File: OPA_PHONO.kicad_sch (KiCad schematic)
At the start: 3 parts, among them J1 Barrel_Jack, J2 Conn_Coaxial_x2, J3 Conn_Coaxial_x2

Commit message: CHANGE POWER SUPPLY
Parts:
- removed J1: Barrel_Jack, Connector_BarrelJack:BarrelJack_CUI_PJ-063AH_Horizontal, symbol Connector:Barrel_Jack
- added J4: USB_C_Receptacle_USB2.0, Connector_USB:USB_C_Receptacle_JAE_DX07S016JA1R1500, symbol Connector:USB_C_Receptacle_USB2.0
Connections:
- net GND: now also J4.A1 (GND), J4.A12 (GND), J4.B1 (GND), J4.B12 (GND), J4.S1 (SHIELD)
- new net POWER/VIN: J4.A4 (VBUS), J4.A9 (VBUS), J4.B4 (VBUS), J4.B9 (VBUS)
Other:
- sheet POWER ports: added VIN; removed AC_A, AC_B

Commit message: update layout
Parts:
- removed J2, J3: Conn_Coaxial_x2, OPA_PHONO:PJRAS2X1S01X, symbol Connector:Conn_Coaxial_x2
- added J1, J2: PJRAS2X1S01X, OPA_PHONO:PJRAS2X1S01X, symbol OPA_PHONO:PJRAS2X1S01X
- J4: value USB_C_Receptacle_USB2.0 -> UJC-HP-3-SMT-TR; footprint Connector_USB:USB_C_Receptacle_JAE_DX07S016JA1R1500 -> Connector_USB:USB_C_Receptacle_Palconn_UTC16-G
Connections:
- net GND: now also J1.S1, J1.S2, J2.S1, J2.S2
- net IN_L: now also J2.T1
- net IN_R: now also J2.T2
- net OUT_L: now also J1.T1
- net OUT_R: now also J1.T2

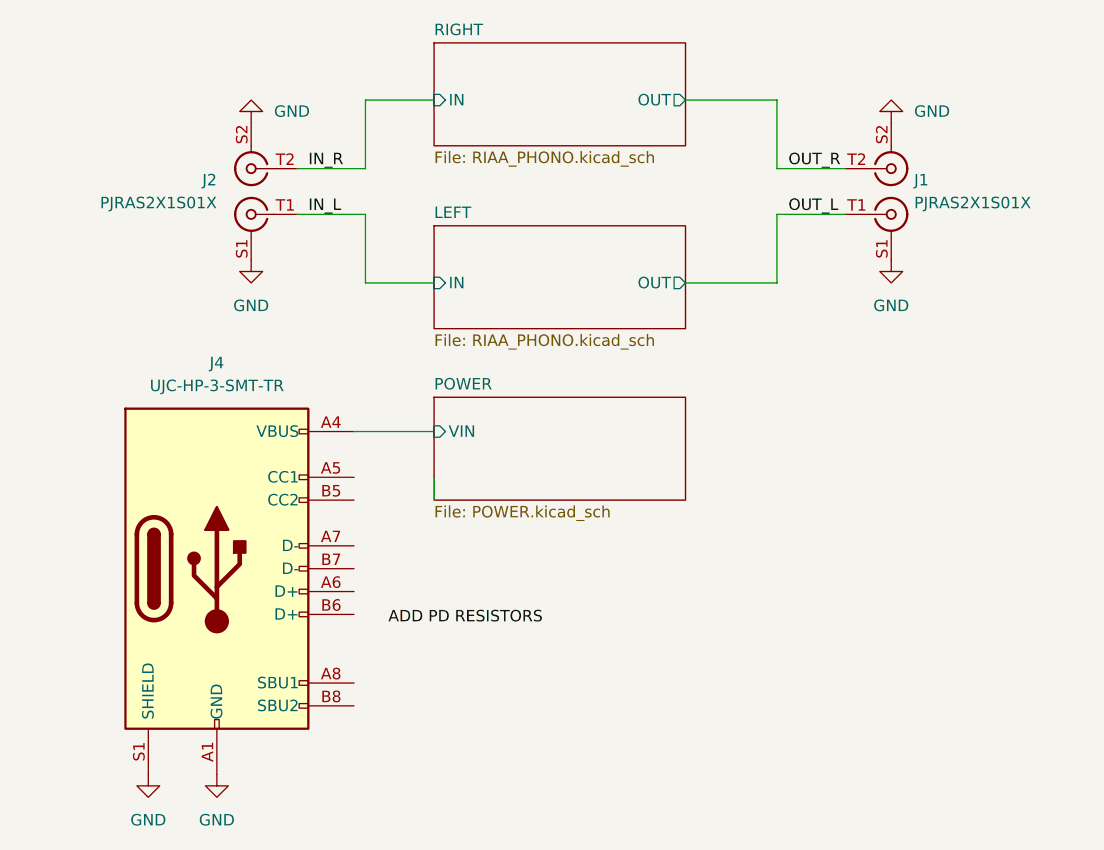
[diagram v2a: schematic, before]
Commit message: add usb c connector
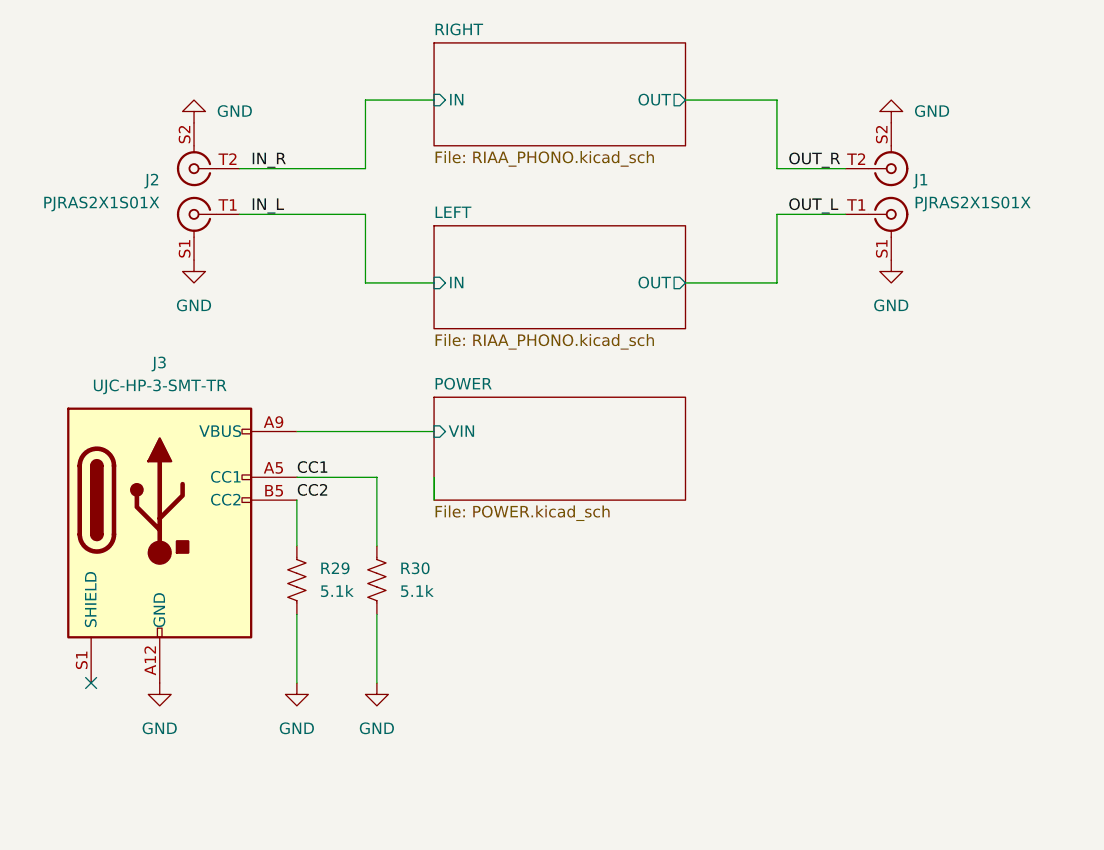
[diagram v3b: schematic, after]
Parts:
- removed J4: UJC-HP-3-SMT-TR, Connector_USB:USB_C_Receptacle_Palconn_UTC16-G, symbol Connector:USB_C_Receptacle_USB2.0
- added J3: UJC-HP-3-SMT-TR, OPA_PHONO:CUI_UJC-HP-3-SMT-TR, symbol OPA_PHONO:UJC-HP-3-SMT-TR
- added R29, R30: 5.1k, Resistor_SMD:R_0402_1005Metric, symbol Device:R_US
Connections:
- net GND: now also J3.A12 (GND), J3.B12 (GND), R29.2, R30.2
- net POWER/VIN: now also J3.A9 (VBUS), J3.B9 (VBUS)
- new net: J3.24 (SHIELD), J3.S1 (SHIELD), J3.S2 (SHIELD), J3.S3 (SHIELD)
- new net CC1: J3.A5 (CC1), R30.1
- new net CC2: J3.B5 (CC2), R29.1
- no-connect marks 0 -> 1
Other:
- moved on the sheet: J2

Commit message: Update component fields
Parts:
- J1, J2: MPN (none) -> PJRAS2X1S01X; Manufacturer (none) -> Switchcraft Inc.
- J3: MPN (none) -> UJC-HP-3-SMT-TR; Manufacturer (none) -> CUI Devices
- R29, R30: MPN (none) -> RC0402FR-075K1L; Manufacturer (none) -> YAGEO
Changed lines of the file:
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@@
+      (effects (font (size 1.27 1.27)) hide)
+    )
+    (property "Description" "CONN DUAL RCA JACK MONO 3.2MM R/A" (id 4) (at 209.55 72.39 0)
+      (effects (font (size 1.27 1.27)) hide)
+    )
+    (property "MPN" "PJRAS2X1S01X" (id 5) (at 209.55 72.39 0)
+      (effects (font (size 1.27 1.27)) hide)
+    )
+    (property "Manufacturer" "Switchcraft Inc." (id 6) (at 209.55 72.39 0)
       (effects (font (size 1.27 1.27)) hide)
     )
@@
       (effects (font (size 1.27 1.27)) hide)
     )
+    (property "Description" "RES SMD 5.1K OHM 1% 1/16W 0402" (id 4) (at 152.4 115.57 0)
+      (effects (font (size 1.27 1.27)) hide)
+    )
+    (property "MPN" "RC0402FR-075K1L" (id 5) (at 152.4 115.57 0)
+      (effects (font (size 1.27 1.27)) hide)
+    )
+    (property "Manufacturer" "YAGEO" (id 6) (at 152.4 115.57 0)
+      (effects (font (size 1.27 1.27)) hide)
+    )
     (pin "1")
     (pin "2")
@@
     )
     (property "Datasheet" "~" (id 3) (at 143.51 115.57 0)
+      (effects (font (size 1.27 1.27)) hide)
+    )
+    (property "Description" "RES SMD 5.1K OHM 1% 1/16W 0402" (id 4) (at 143.51 115.57 0)
+      (effects (font (size 1.27 1.27)) hide)
+    )
+    (property "MPN" "RC0402FR-075K1L" (id 5) (at 143.51 115.57 0)
+      (effects (font (size 1.27 1.27)) hide)
+    )
+    (property "Manufacturer" "YAGEO" (id 6) (at 143.51 115.57 0)
       (effects (font (size 1.27 1.27)) hide)
     )
@@
     )
     (property "Datasheet" "https://www.usb.org/sites/default/files/documents/usb_type-c.zip" (id 3) (at 130.81 104.14 0)
+      (effects (font (size 1.27 1.27)) hide)
+    )
+    (property "Description" "CONN RCPT TYPE C 24POS SMD RA" (id 4) (at 128.27 114.3 0)
+      (effects (font (size 1.27 1.27)) hide)
+    )
+    (property "MPN" "UJC-HP-3-SMT-TR" (id 5) (at 128.27 114.3 0)
+      (effects (font (size 1.27 1.27)) hide)
+    )
+    (property "Manufacturer" "CUI Devices" (id 6) (at 128.27 114.3 0)
       (effects (font (size 1.27 1.27)) hide)
     )
@@
       (effects (font (size 1.27 1.27)) hide)
     )
+    (property "Description" "CONN DUAL RCA JACK MONO 3.2MM R/A" (id 4) (at 132.08 72.39 0)
+      (effects (font (size 1.27 1.27)) hide)
+    )
+    (property "MPN" "PJRAS2X1S01X" (id 5) (at 132.08 72.39 0)
+      (effects (font (size 1.27 1.27)) hide)
+    )
+    (property "Manufacturer" "Switchcraft Inc." (id 6) (at 132.08 72.39 0)
+      (effects (font (size 1.27 1.27)) hide)
+    )
     (pin "S2")
     (pin "T1")
@@
     )
     (path "/b71452ae-e2ec-4238-9d16-71d9677f964c/3401a4bc-8750-45f7-8ad3-ee304a81e512"
-      (reference "C2") (unit 1) (value "68n") (footprint "Capacitor_SMD:C_1206_3216Metric")
+      (reference "C2") (unit 1) (value "68n") (footprint "Capacitor_SMD:C_1210_3225Metric")
     )
     (path "/b71452ae-e2ec-4238-9d16-71d9677f964c/e7e337ea-d0d4-4479-a2c0-823fa5bff63a"
-      (reference "C3") (unit 1) (value "68n") (footprint "Capacitor_SMD:C_1206_3216Metric")
+      (reference "C3") (unit 1) (value "68n") (footprint "Capacitor_SMD:C_1210_3225Metric")
     )
     (path "/b71452ae-e2ec-4238-9d16-71d9677f964c/47e616e0-9f9d-4905-87b6-b1f7ea1d9240"
@@
     )
     (path "/c67bced7-2ecb-4fda-afd4-a12d6372c9ce/3401a4bc-8750-45f7-8ad3-ee304a81e512"
-      (reference "C8") (unit 1) (value "68n") (footprint "Capacitor_SMD:C_1206_3216Metric")
+      (reference "C8") (unit 1) (value "68n") (footprint "Capacitor_SMD:C_1210_3225Metric")
     )
     (path "/c67bced7-2ecb-4fda-afd4-a12d6372c9ce/e7e337ea-d0d4-4479-a2c0-823fa5bff63a"
-      (reference "C9") (unit 1) (value "68n") (footprint "Capacitor_SMD:C_1206_3216Metric")
+      (reference "C9") (unit 1) (value "68n") (footprint "Capacitor_SMD:C_1210_3225Metric")
     )
     (path "/c67bced7-2ecb-4fda-afd4-a12d6372c9ce/47e616e0-9f9d-4905-87b6-b1f7ea1d9240"
@@
     )
     (path "/54617677-cfc6-4c88-8682-59d8a487d34d/012ce2e0-2b16-46fe-aa72-a30f8cf3f1ba"
-      (reference "C19") (unit 1) (value "1u") (footprint "Capacitor_SMD:C_0402_1005Metric")
+      (reference "C19") (unit 1) (value "4.7u") (footprint "Capacitor_SMD:C_0402_1005Metric")
     )
     (path "/54617677-cfc6-4c88-8682-59d8a487d34d/8b3b6e42-30ae-4787-975f-1307bbc78122"
-      (reference "C20") (unit 1) (value "1u") (footprint "Capacitor_SMD:C_0402_1005Metric")
+      (reference "C20") (unit 1) (value "4.7u") (footprint "Capacitor_SMD:C_0402_1005Metric")
     )
     (path "/54617677-cfc6-4c88-8682-59d8a487d34d/b865ef55-d049-44bf-9f62-477ce371aff2"
-      (reference "C21") (unit 1) (value "1u") (footprint "Capacitor_SMD:C_0402_1005Metric")
+      (reference "C21") (unit 1) (value "4.7u") (footprint "Capacitor_SMD:C_0402_1005Metric")
     )
     (path "/54617677-cfc6-4c88-8682-59d8a487d34d/7481d368-de94-4cfa-8658-752acc214285"
-      (reference "C22") (unit 1) (value "1u") (footprint "Capacitor_SMD:C_0402_1005Metric")
+      (reference "C22") (unit 1) (value "4.7u") (footprint "Capacitor_SMD:C_0402_1005Metric")
     )
     (path "/54617677-cfc6-4c88-8682-59d8a487d34d/d015ac9c-8503-428f-b611-918e99cff21b"
@@
     )
     (path "/b71452ae-e2ec-4238-9d16-71d9677f964c/2a4ad1e3-8d24-4e7f-868b-1019aa3d2553"
-      (reference "R1") (unit 1) (value "R_US") (footprint "Resistor_SMD:R_0402_1005Metric")
+      (reference "R1") (unit 1) (value "47k") (footprint "Resistor_SMD:R_0402_1005Metric")
     )
     (path "/b71452ae-e2ec-4238-9d16-71d9677f964c/b777cf12-c2ab-48a2-93f0-242f456945c9"
@@
     )
     (path "/c67bced7-2ecb-4fda-afd4-a12d6372c9ce/2a4ad1e3-8d24-4e7f-868b-1019aa3d2553"
-      (reference "R13") (unit 1) (value "R_US") (footprint "Resistor_SMD:R_0402_1005Metric")
+      (reference "R13") (unit 1) (value "47k") (footprint "Resistor_SMD:R_0402_1005Metric")
     )
     (path "/c67bced7-2ecb-4fda-afd4-a12d6372c9ce/b777cf12-c2ab-48a2-93f0-242f456945c9"

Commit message: Clean DRC
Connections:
- now unconnected: J3.S1 (SHIELD), J3.S2 (SHIELD), J3.S3 (SHIELD)
- no-connect marks 1 -> 4
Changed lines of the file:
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@@
   (paper "A4")
   (no_connect (at 120.65 127))
+  (no_connect (at 123.19 127))
+  (no_connect (at 133.35 127))
+  (no_connect (at 135.89 127))
   (wire (pts (xy 196.85 69.85) (xy 204.47 69.85))
     (stroke (width 0) (type default) (color 0 0 0 0))
@@
     (pin "2")
   )
-  (symbol (lib_id "power:GND") (at 132.08 64.77 180) (unit 1)
-    (in_bom yes) (on_board yes) (fields_autoplaced)
-    (property "Reference" "#PWR0104" (id 0) (at 132.08 58.42 0)
-      (effects (font (size 1.27 1.27)) hide)
-    )
-    (property "Value" "GND" (id 1) (at 134.62 63.4999 0)
-      (effects (font (size 1.27 1.27)) (justify right))
-    )
-    (property "Footprint" "" (id 2) (at 132.08 64.77 0)
-      (effects (font (size 1.27 1.27)) hide)
-    )
-    (property "Datasheet" "" (id 3) (at 132.08 64.77 0)
-      (effects (font (size 1.27 1.27)) hide)
-    )
-    (pin "1")
-  )
-  (symbol (lib_id "power:GND") (at 132.08 80.01 0) (unit 1)
-    (in_bom yes) (on_board yes) (fields_autoplaced)
-    (property "Reference" "#PWR03" (id 0) (at 132.08 86.36 0)
-      (effects (font (size 1.27 1.27)) hide)
-    )
-    (property "Value" "GND" (id 1) (at 132.08 85.09 0))
-    (property "Footprint" "" (id 2) (at 132.08 80.01 0)
-      (effects (font (size 1.27 1.27)) hide)
-    )
-    (property "Datasheet" "" (id 3) (at 132.08 80.01 0)
-      (effects (font (size 1.27 1.27)) hide)
-    )
-    (pin "1")
-  )
-  (symbol (lib_id "Device:R_US") (at 143.51 115.57 0) (unit 1)
-    (in_bom yes) (on_board yes) (fields_autoplaced)
-    (property "Reference" "R29" (id 0) (at 146.05 114.2999 0)
-      (effects (font (size 1.27 1.27)) (justify left))
-    )
-    (property "Value" "5.1k" (id 1) (at 146.05 116.8399 0)
-      (effects (font (size 1.27 1.27)) (justify left))
-    )
-    (property "Footprint" "Resistor_SMD:R_0402_1005Metric" (id 2) (at 144.526 115.824 90)
-      (effects (font (size 1.27 1.27)) hide)
-    )
-    (property "Datasheet" "~" (id 3) (at 143.51 115.57 0)
-      (effects (font (size 1.27 1.27)) hide)
-    )
-    (property "Description" "RES SMD 5.1K OHM 1% 1/16W 0402" (id 4) (at 143.51 115.57 0)
-      (effects (font (size 1.27 1.27)) hide)
-    )
-    (property "MPN" "RC0402FR-075K1L" (id 5) (at 143.51 115.57 0)
-      (effects (font (size 1.27 1.27)) hide)
-    )
-    (property "Manufacturer" "YAGEO" (id 6) (at 143.51 115.57 0)
-      (effects (font (size 1.27 1.27)) hide)
-    )
-    (pin "1")
-    (pin "2")
-  )
-  (symbol (lib_id "power:GND") (at 209.55 64.77 180) (unit 1)
-    (in_bom yes) (on_board yes) (fields_autoplaced)
-    (property "Reference" "#PWR0103" (id 0) (at 209.55 58.42 0)
-      (effects (font (size 1.27 1.27)) hide)
-    )
-    (property "Value" "GND" (id 1) (at 212.09 63.4999 0)
-      (effects (font (size 1.27 1.27)) (justify right))
-    )
-    (property "Footprint" "" (id 2) (at 209.55 64.77 0)
-      (effects (font (size 1.27 1.27)) hide)
-    )
-    (property "Datasheet" "" (id 3) (at 209.55 64.77 0)
-      (effects (font (size 1.27 1.27)) hide)
-    )
-    (pin "1")
-  )
-  (symbol (lib_id "power:GND") (at 209.55 80.01 0) (unit 1)
-    (in_bom yes) (on_board yes) (fields_autoplaced)
-    (property "Reference" "#PWR04" (id 0) (at 209.55 86.36 0)
-      (effects (font (size 1.27 1.27)) hide)
-    )
-    (property "Value" "GND" (id 1) (at 209.55 85.09 0))
-    (property "Footprint" "" (id 2) (at 209.55 80.01 0)
-      (effects (font (size 1.27 1.27)) hide)
-    )
-    (property "Datasheet" "" (id 3) (at 209.55 80.01 0)
-      (effects (font (size 1.27 1.27)) hide)
-    )
-    (pin "1")
-  )
   (symbol (lib_id "OPA_PHONO:UJC-HP-3-SMT-TR") (at 128.27 114.3 0) (unit 1)
     (in_bom yes) (on_board yes) (fields_autoplaced)
@@
       (effects (font (size 1.27 1.27)) hide)
     )
-    (pin "24")
+    (pin "S4")
     (pin "A12")
     (pin "A5")
@@
     (pin "S3")
   )
+  (symbol (lib_id "power:GND") (at 132.08 64.77 180) (unit 1)
+    (in_bom yes) (on_board yes) (fields_autoplaced)
+    (property "Reference" "#PWR0104" (id 0) (at 132.08 58.42 0)
+      (effects (font (size 1.27 1.27)) hide)
+    )
+    (property "Value" "GND" (id 1) (at 134.62 63.4999 0)
+      (effects (font (size 1.27 1.27)) (justify right))
+    )
+    (property "Footprint" "" (id 2) (at 132.08 64.77 0)
+      (effects (font (size 1.27 1.27)) hide)
+    )
+    (property "Datasheet" "" (id 3) (at 132.08 64.77 0)
+      (effects (font (size 1.27 1.27)) hide)
+    )
+    (pin "1")
+  )
+  (symbol (lib_id "power:GND") (at 132.08 80.01 0) (unit 1)
+    (in_bom yes) (on_board yes) (fields_autoplaced)
+    (property "Reference" "#PWR03" (id 0) (at 132.08 86.36 0)
+      (effects (font (size 1.27 1.27)) hide)
+    )
+    (property "Value" "GND" (id 1) (at 132.08 85.09 0))
+    (property "Footprint" "" (id 2) (at 132.08 80.01 0)
+      (effects (font (size 1.27 1.27)) hide)
+    )
+    (property "Datasheet" "" (id 3) (at 132.08 80.01 0)
+      (effects (font (size 1.27 1.27)) hide)
+    )
+    (pin "1")
+  )
+  (symbol (lib_id "Device:R_US") (at 143.51 115.57 0) (unit 1)
+    (in_bom yes) (on_board yes) (fields_autoplaced)
+    (property "Reference" "R29" (id 0) (at 146.05 114.2999 0)
+      (effects (font (size 1.27 1.27)) (justify left))
+    )
+    (property "Value" "5.1k" (id 1) (at 146.05 116.8399 0)
+      (effects (font (size 1.27 1.27)) (justify left))
+    )
+    (property "Footprint" "Resistor_SMD:R_0402_1005Metric" (id 2) (at 144.526 115.824 90)
+      (effects (font (size 1.27 1.27)) hide)
+    )
+    (property "Datasheet" "~" (id 3) (at 143.51 115.57 0)
+      (effects (font (size 1.27 1.27)) hide)
+    )
+    (property "Description" "RES SMD 5.1K OHM 1% 1/16W 0402" (id 4) (at 143.51 115.57 0)
+      (effects (font (size 1.27 1.27)) hide)
+    )
+    (property "MPN" "RC0402FR-075K1L" (id 5) (at 143.51 115.57 0)
+      (effects (font (size 1.27 1.27)) hide)
+    )
+    (property "Manufacturer" "YAGEO" (id 6) (at 143.51 115.57 0)
+      (effects (font (size 1.27 1.27)) hide)
+    )
+    (pin "1")
+    (pin "2")
+  )
+  (symbol (lib_id "power:GND") (at 209.55 64.77 180) (unit 1)
+    (in_bom yes) (on_board yes) (fields_autoplaced)
+    (property "Reference" "#PWR0103" (id 0) (at 209.55 58.42 0)
+      (effects (font (size 1.27 1.27)) hide)
+    )
+    (property "Value" "GND" (id 1) (at 212.09 63.4999 0)
+      (effects (font (size 1.27 1.27)) (justify right))
+    )
+    (property "Footprint" "" (id 2) (at 209.55 64.77 0)
+      (effects (font (size 1.27 1.27)) hide)
+    )
+    (property "Datasheet" "" (id 3) (at 209.55 64.77 0)
+      (effects (font (size 1.27 1.27)) hide)
+    )
+    (pin "1")
+  )
+  (symbol (lib_id "power:GND") (at 209.55 80.01 0) (unit 1)
+    (in_bom yes) (on_board yes) (fields_autoplaced)
+    (property "Reference" "#PWR04" (id 0) (at 209.55 86.36 0)
+      (effects (font (size 1.27 1.27)) hide)
+    )
+    (property "Value" "GND" (id 1) (at 209.55 85.09 0))
+    (property "Footprint" "" (id 2) (at 209.55 80.01 0)
+      (effects (font (size 1.27 1.27)) hide)
+    )
+    (property "Datasheet" "" (id 3) (at 209.55 80.01 0)
+      (effects (font (size 1.27 1.27)) hide)
+    )
+    (pin "1")
+  )
   (symbol (lib_id "OPA_PHONO:PJRAS2X1S01X") (at 132.08 72.39 180) (unit 1)
     (in_bom yes) (on_board yes) (fields_autoplaced)
@@
       (reference "J2") (unit 1) (value "PJRAS2X1S01X") (footprint "OPA_PHONO:PJRAS2X1S01X")
     )
-    (path "/d18077bb-6fb4-4daf-b6ee-2ecd9b055d59"
+    (path "/6a41d364-e7d5-4400-beef-f6f5f8c70d7f"
       (reference "J3") (unit 1) (value "UJC-HP-3-SMT-TR") (footprint "OPA_PHONO:CUI_UJC-HP-3-SMT-TR")
     )
